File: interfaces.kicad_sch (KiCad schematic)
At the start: 92 parts, among them IC6001 TPD8S009DSMR, J6001 HDMI_A_Female_685119134923, J6002 USB-C_USB4105-GF-A, J6003 MicroSD_693071020811, Q6001 BSS138PW, Q6002 BSS138PW, Q6003 BSS138PW, Q6004 BSS138PW, Q6005 BSS138PW, Q6006 BSS138PW, Q6007 BSS138PW, Q6008 BSS138PW, U6001 FT4232H_VQFN, Y6001 Oscillator_SMD_12MHz_KX-7

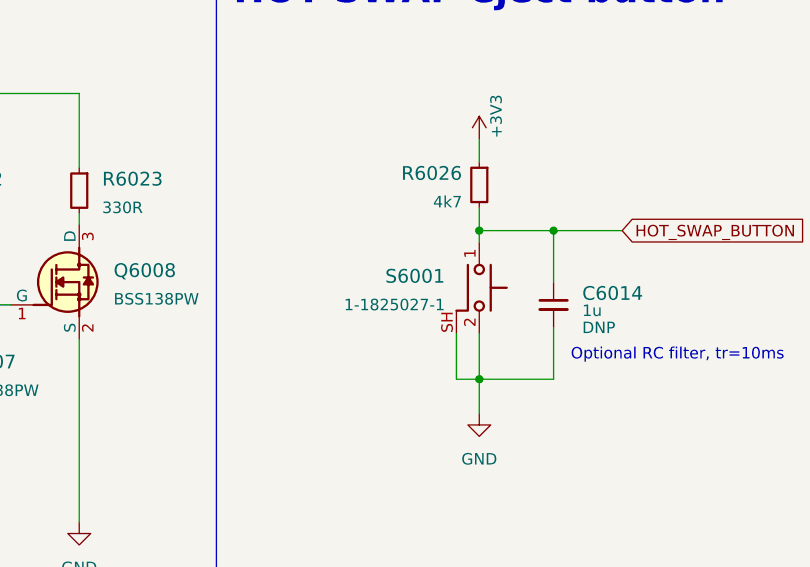
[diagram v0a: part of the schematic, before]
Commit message: Schematic cleanup, connect VINT DC-DC, continue placing misc. circuits
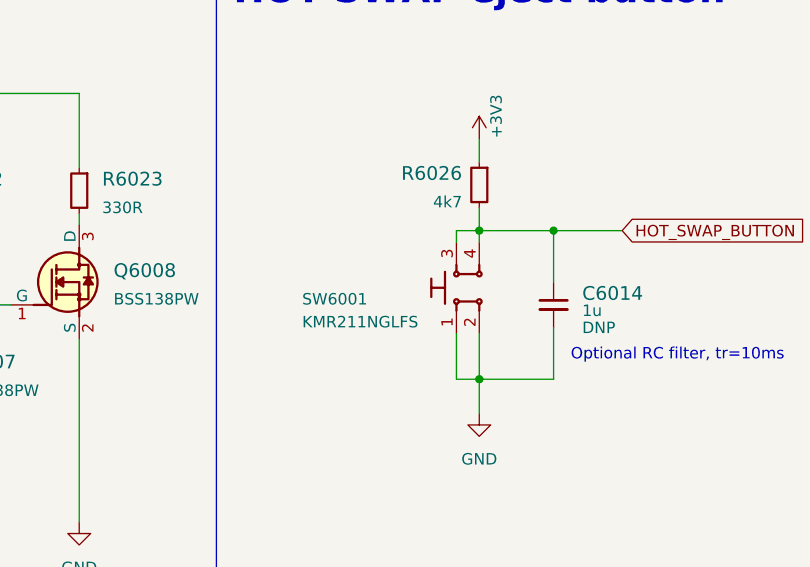
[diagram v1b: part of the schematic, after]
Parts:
- removed S6001: SW_1-1825027-1, data-center-rdimm-ddr4-tester-footprints:SW_Tactile_SPST_Angled_TE_1825027, symbol data-center-rdimm-ddr4-tester:SW_1-1825027-1
- added SW6001: SW_KMR211NGLFS_SMD, antmicro-footprints:SW_KMR211NGLFS_SMD, symbol antmicroPushbuttonSwitches:SW_KMR211NGLFS_SMD
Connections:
- net GND: now also SW6001.1, SW6001.2
- net HOT_SWAP_BUTTON: now also SW6001.3, SW6001.4
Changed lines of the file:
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@@
     (stroke (width 0) (type default) (color 0 0 0 0))
   )
+  (wire (pts (xy 256.54 245.11) (xy 256.54 246.38))
+    (stroke (width 0) (type default) (color 0 0 0 0))
+  )
   (wire (pts (xy 375.92 99.06) (xy 375.92 101.6))
     (stroke (width 0) (type default) (color 0 0 0 0))
@@
     (stroke (width 0) (type default) (color 0 0 0 0))
   )
+  (wire (pts (xy 259.08 245.11) (xy 256.54 245.11))
+    (stroke (width 0) (type default) (color 0 0 0 0))
+  )
   (wire (pts (xy 41.275 74.295) (xy 48.26 74.295))
     (stroke (width 0) (type default) (color 0 0 0 0))
@@
     (pin "SH")
   )
+  (symbol (lib_id "antmicroPushbuttonSwitches:SW_KMR211NGLFS_SMD") (at 256.54 256.54 90) (unit 1)
+    (in_bom yes) (on_board yes)
+    (property "Reference" "SW6001" (id 0) (at 239.395 252.73 90)
+      (effects (font (size 1.27 1.27) (thickness 0.15)) (justify right))
+    )
+    (property "Value" "SW_KMR211NGLFS_SMD" (id 1) (at 264.16 231.14 0)
+      (effects (font (size 1.27 1.27) (thickness 0.15)) (justify left bottom) hide)
+    )
+    (property "Footprint" "antmicro-footprints:SW_KMR211NGLFS_SMD" (id 2) (at 266.7 231.14 0)
+      (effects (font (size 1.27 1.27) (thickness 0.15)) (justify left bottom) hide)
+    )
+    (property "Datasheet" "http://www.farnell.com/datasheets/2631211.pdf" (id 3) (at 269.24 231.14 0)
+      (effects (font (size 1.27 1.27) (thickness 0.15)) (justify left bottom) hide)
+    )
+    (property "MPN" "KMR211NGLFS" (id 4) (at 239.395 255.27 90)
+      (effects (font (size 1.27 1.27) (thickness 0.15)) (justify right))
+    )
+    (property "Manufacturer" "C&K" (id 5) (at 271.78 231.14 0)
+      (effects (font (size 1.27 1.27) (thickness 0.15)) (justify left bottom) hide)
+    )
+    (property "Author" "Antmicro" (id 6) (at 274.32 231.14 0)
+      (effects (font (size 1.27 1.27) (thickness 0.15)) (justify left bottom) hide)
+    )
+    (property "License" "Apache-2.0" (id 7) (at 276.86 231.14 0)
+      (effects (font (size 1.27 1.27) (thickness 0.15)) (justify left bottom) hide)
+    )
+    (pin "1")
+    (pin "2")
+    (pin "3")
+    (pin "4")
+  )
   (symbol (lib_id "power:+3V3") (at 80.645 235.585 90) (unit 1)
     (in_bom yes) (on_board yes)
@@
     (pin "1")
   )
-  (symbol (lib_id "data-center-rdimm-ddr4-tester:SW_1-1825027-1") (at 260.35 246.38 270) (unit 1)
-    (in_bom yes) (on_board yes) (fields_autoplaced)
-    (property "Reference" "S6001" (id 0) (at 255.27 250.19 90)
-      (effects (font (size 1.524 1.524)) (justify right))
-    )
-    (property "Value" "SW_1-1825027-1" (id 1) (at 254.635 253.3649 90)
-      (effects (font (size 1.27 1.27) (thickness 0.15)) (justify right) hide)
-    )
-    (property "Footprint" "data-center-rdimm-ddr4-tester-footprints:SW_Tactile_SPST_Angled_TE_1825027" (id 2) (at 250.19 271.78 0)
-      (effects (font (size 1.27 1.27) (thickness 0.15)) (justify left bottom) hide)
-    )
-    (property "Datasheet" "https://www.te.com/commerce/DocumentDelivery/DDEController?Action=showdoc&DocId=Customer+Drawing%7F1825027%7FH1%7Fpdf%7FEnglish%7FENG_CD_1825027_H1.pdf%7F1-1825027-1" (id 3) (at 247.65 271.78 0)
-      (effects (font (size 1.27 1.27) (thickness 0.15)) (justify left bottom) hide)
-    )
-    (property "MPN" "1-1825027-1" (id 4) (at 255.27 253.3649 90)
-      (effects (font (size 1.27 1.27) (thickness 0.15)) (justify right))
-    )
-    (property "Manufacturer" "TE Connectivity" (id 5) (at 242.57 271.78 0)
-      (effects (font (size 1.27 1.27) (thickness 0.15)) (justify left bottom) hide)
-    )
-    (property "Author" "Antmicro" (id 6) (at 240.03 271.78 0)
-      (effects (font (size 1.27 1.27) (thickness 0.15)) (justify left bottom) hide)
-    )
-    (property "License" "Apache-2.0" (id 7) (at 237.49 271.78 0)
-      (effects (font (size 1.27 1.27) (thickness 0.15)) (justify left bottom) hide)
-    )
-    (pin "1")
-    (pin "2")
-    (pin "SH")
-  )
   (symbol (lib_id "data-center-rdimm-ddr4-tester:BSS138PW") (at 170.18 273.685 0) (unit 1)

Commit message: Add loclib
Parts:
- C6001, C6003, C6005, C6008, C6009, C6010, C6012, C6013, C6016, C6017: footprint data-center-rdimm-ddr4-tester-footprints:C_0402_1005Metric -> sodimm-ddr5-tester-footprints:C_0402_1005Metric; symbol data-center-rdimm-ddr4-tester:C_100n_0402 -> sodimm-ddr5-tester:C_100n_0402
- C6002, C6007: footprint data-center-rdimm-ddr4-tester-footprints:C_0402_1005Metric -> sodimm-ddr5-tester-footprints:C_0402_1005Metric; symbol data-center-rdimm-ddr4-tester:C_18p_0402 -> sodimm-ddr5-tester:C_18p_0402
- C6004, C6006, C6011: footprint data-center-rdimm-ddr4-tester-footprints:C_0402_1005Metric -> sodimm-ddr5-tester-footprints:C_0402_1005Metric; symbol data-center-rdimm-ddr4-tester:C_4u7_0402 -> sodimm-ddr5-tester:C_4u7_0402
- C6014, C6015: footprint data-center-rdimm-ddr4-tester-footprints:C_0402_1005Metric -> sodimm-ddr5-tester-footprints:C_0402_1005Metric; symbol data-center-rdimm-ddr4-tester:C_1u_0402 -> sodimm-ddr5-tester:C_1u_0402
- D6001, D6002, D6003, D6004, D6005: footprint data-center-rdimm-ddr4-tester-footprints:LED_0603_1608Metric_G -> sodimm-ddr5-tester-footprints:LED_0603_1608Metric_G; symbol data-center-rdimm-ddr4-tester:LED_G_0603_KP-1608CGCK -> sodimm-ddr5-tester:LED_G_0603_KP-1608CGCK
- D6006: footprint data-center-rdimm-ddr4-tester-footprints:LED_RGY_1.6x1.6mm_APTF1616 -> sodimm-ddr5-tester-footprints:LED_RGY_1.6x1.6mm_APTF1616; symbol data-center-rdimm-ddr4-tester:LED_RGY_0606_APTF1616SURKCGKSYKC -> sodimm-ddr5-tester:LED_RGY_0606_APTF1616SURKCGKSYKC
- D6007: footprint data-center-rdimm-ddr4-tester-footprints:SOT-723 -> sodimm-ddr5-tester-footprints:SOT-723; symbol data-center-rdimm-ddr4-tester:TPD2E009_SOT-9X3 -> sodimm-ddr5-tester:TPD2E009_SOT-9X3
- FB6001, FB6002: footprint data-center-rdimm-ddr4-tester-footprints:FB_0603_1608Metric -> sodimm-ddr5-tester-footprints:FB_0603_1608Metric; symbol data-center-rdimm-ddr4-tester:FB_600Z_0.5A_0603 -> sodimm-ddr5-tester:FB_600Z_0.5A_0603
- IC6001: footprint data-center-rdimm-ddr4-tester-footprints:R-PDSO-N15 -> sodimm-ddr5-tester-footprints:R-PDSO-N15; symbol data-center-rdimm-ddr4-tester:TPD8S009DSMR -> sodimm-ddr5-tester:TPD8S009DSMR
- J6001: footprint data-center-rdimm-ddr4-tester-footprints:HDMI-A_Wurth_685119134923 -> sodimm-ddr5-tester-footprints:HDMI-A_Wurth_685119134923; symbol data-center-rdimm-ddr4-tester:HDMI_A_Female_685119134923 -> sodimm-ddr5-tester:HDMI_A_Female_685119134923
- J6002: footprint data-center-rdimm-ddr4-tester-footprints:USB-C_GCT_USB4105-GF-A -> sodimm-ddr5-tester-footprints:USB-C_GCT_USB4105-GF-A; symbol data-center-rdimm-ddr4-tester:USB-C_USB4105-GF-A -> sodimm-ddr5-tester:USB-C_USB4105-GF-A
- J6003: footprint data-center-rdimm-ddr4-tester-footprints:MicroSD_Wurth_693071020811 -> sodimm-ddr5-tester-footprints:MicroSD_Wurth_693071020811; symbol data-center-rdimm-ddr4-tester:MicroSD_693071020811 -> sodimm-ddr5-tester:MicroSD_693071020811
- Q6001, Q6002, Q6003, Q6004, Q6005, Q6006, Q6007, Q6008: footprint data-center-rdimm-ddr4-tester-footprints:SC70-3 -> sodimm-ddr5-tester-footprints:SC70-3; symbol data-center-rdimm-ddr4-tester:BSS138PW -> sodimm-ddr5-tester:BSS138PW
- R6001, R6002, R6003, R6006, R6007, R6021, R6022, R6023, R6043, R6044: footprint data-center-rdimm-ddr4-tester-footprints:R_0402_1005Metric -> sodimm-ddr5-tester-footprints:R_0402_1005Metric; symbol data-center-rdimm-ddr4-tester:R_330R_0402 -> sodimm-ddr5-tester:R_330R_0402
- R6004: footprint data-center-rdimm-ddr4-tester-footprints:R_0402_1005Metric -> sodimm-ddr5-tester-footprints:R_0402_1005Metric; symbol data-center-rdimm-ddr4-tester:R_10k_0402 -> sodimm-ddr5-tester:R_10k_0402
- R6005: footprint data-center-rdimm-ddr4-tester-footprints:R_0402_1005Metric -> sodimm-ddr5-tester-footprints:R_0402_1005Metric; symbol data-center-rdimm-ddr4-tester:R_12k_0402 -> sodimm-ddr5-tester:R_12k_0402
- R6008, R6009, R6010, R6011, R6012, R6013, R6014, R6015, R6016, R6017, R6018, R6019, R6020: footprint data-center-rdimm-ddr4-tester-footprints:R_0402_1005Metric -> sodimm-ddr5-tester-footprints:R_0402_1005Metric; symbol data-center-rdimm-ddr4-tester:R_22R_0402 -> sodimm-ddr5-tester:R_22R_0402
- R6024, R6025: footprint data-center-rdimm-ddr4-tester-footprints:R_0402_1005Metric -> sodimm-ddr5-tester-footprints:R_0402_1005Metric; symbol data-center-rdimm-ddr4-tester:R_5k11_0402 -> sodimm-ddr5-tester:R_5k11_0402
- R6026: footprint data-center-rdimm-ddr4-tester-footprints:R_0402_1005Metric -> sodimm-ddr5-tester-footprints:R_0402_1005Metric; symbol data-center-rdimm-ddr4-tester:R_4k7_0402 -> sodimm-ddr5-tester:R_4k7_0402
- R6027, R6028, R6029, R6030, R6032, R6035, R6038, R6041: footprint data-center-rdimm-ddr4-tester-footprints:R_0402_1005Metric -> sodimm-ddr5-tester-footprints:R_0402_1005Metric; symbol data-center-rdimm-ddr4-tester:R_0R_0402 -> sodimm-ddr5-tester:R_0R_0402
- R6031, R6033, R6034, R6036, R6039, R6040, R6042: footprint data-center-rdimm-ddr4-tester-footprints:R_0402_1005Metric -> sodimm-ddr5-tester-footprints:R_0402_1005Metric; symbol data-center-rdimm-ddr4-tester:R_20k_0402 -> sodimm-ddr5-tester:R_20k_0402
- R6037: footprint data-center-rdimm-ddr4-tester-footprints:R_0402_1005Metric -> sodimm-ddr5-tester-footprints:R_0402_1005Metric; symbol data-center-rdimm-ddr4-tester:R_220R_0402 -> sodimm-ddr5-tester:R_220R_0402
- SW6001: footprint antmicro-footprints:SW_KMR211NGLFS_SMD -> sodimm-ddr5-tester-footprints:SW_KMR211NGLFS_SMD; symbol antmicroPushbuttonSwitches:SW_KMR211NGLFS_SMD -> sodimm-ddr5-tester:SW_KMR211NGLFS_SMD
- TP6001, TP6002, TP6003, TP6004, TP6005, TP6006, VBUS6001: footprint data-center-rdimm-ddr4-tester-footprints:Testpoint_smd_1mm -> sodimm-ddr5-tester-footprints:Testpoint_smd_1mm; symbol data-center-rdimm-ddr4-tester:TP_1mm_SMD -> sodimm-ddr5-tester:TP_1mm_SMD
- U6001: footprint data-center-rdimm-ddr4-tester-footprints:QFN-56-1EP_8x8mm_P0.5mm -> sodimm-ddr5-tester-footprints:QFN-56-1EP_8x8mm_P0.5mm; symbol data-center-rdimm-ddr4-tester:FT4232H_VQFN -> sodimm-ddr5-tester:FT4232H_VQFN
- Y6001: footprint data-center-rdimm-ddr4-tester-footprints:Oscillator_SMD_Geyer_KX-7-4Pin_3.2x2.5mm -> sodimm-ddr5-tester-footprints:Oscillator_SMD_Geyer_KX-7-4Pin_3.2x2.5mm; symbol data-center-rdimm-ddr4-tester:Oscillator_SMD_12MHz_KX-7 -> sodimm-ddr5-tester:Oscillator_SMD_12MHz_KX-7

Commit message: Bump revision to 1.0.0
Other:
- title: LPDDR5 Test Board -> SO-DIMM DDR5 Tester

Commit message: Connect RFU, start improving interfaces and supply sheet, unify ESD protection
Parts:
- removed D6007: TPD2E009_SOT-9X3, sodimm-ddr5-tester-footprints:SOT-723, symbol sodimm-ddr5-tester:TPD2E009_SOT-9X3
- removed IC6001: TPD8S009DSMR, sodimm-ddr5-tester-footprints:R-PDSO-N15, symbol sodimm-ddr5-tester:TPD8S009DSMR
- removed J6001: HDMI_A_Female_685119134923, sodimm-ddr5-tester-footprints:HDMI-A_Wurth_685119134923, symbol sodimm-ddr5-tester:HDMI_A_Female_685119134923
- added C?: C_10u_25V_0603, antmicro-footprints:C_0603_1608Metric, symbol antmicroCapacitors0603:C_10u_25V_0603
- added C? (x2): C_100n_0402_EIA, K410T-devboard-footprints:C_0402_1005Metric_EIA, symbol K410T-devboard:C_100n_0402_EIA
- added C?: C_10u_0402, antmicro-footprints:C_0402_1005Metric, symbol antmicroCapacitors0402:C_10u_0402
- added D? (x2): BAT54-02V-G3-08, antmicro-footprints:SOD-523, symbol antmicroDiodesRectifiersSingle:BAT54-02V-G3-08
- added D? (x4): LED_G_0603_KP-1608CGCK, sodimm-ddr5-tester-footprints:LED_0603_1608Metric_G, symbol sodimm-ddr5-tester:LED_G_0603_KP-1608CGCK
- added FB?: FB_120Z_2A_0603, K410T-devboard-footprints:FB_0603_1608Metric, symbol K410T-devboard:FB_120Z_2A_0603
- added J6001: HDMI-A_WE_685119134923, antmicro-footprints:HDMI-A_Receptacle_WE_685119134923, symbol antmicroVideoConnectors:HDMI-A_WE_685119134923
- added R? (x4): R_0R_0402, antmicro-footprints:R_0402_1005Metric, symbol antmicroResistors0402:R_0R_0402
- added R? (x4): R_330R_0402, antmicro-footprints:R_0402_1005Metric, symbol antmicroResistors0402:R_330R_0402
- added R?: R_47k_0402, antmicro-footprints:R_0402_1005Metric, symbol antmicroResistors0402:R_47k_0402
- added R?: R_10k_0402, antmicro-footprints:R_0402_1005Metric, symbol antmicroResistors0402:R_10k_0402
- added U? (x2): TXU0304BQAR, antmicro-footprints:DHVQFN-14_1EP_2.5x3mm, symbol antmicroLogicTranslatorsLevelShifters:TXU0304BQAR
- added U?: NCP718BSN330T1G, antmicro-footprints:SOT-23-5, symbol antmicroPMICVoltageRegulatorsLinear:NCP718BSN330T1G
- added U? (x3): TPD4E05U06QDQARQ1, antmicro-footprints:USON-10_2.5x1mm_P0.5mm, symbol antmicroTVSDiodes:TPD4E05U06QDQARQ1
- added U?: SN74HC595B, antmicro-footprints:X1QFN-16-1EP_2.5x2.5mm, symbol antmicroLogicShiftRegisters:SN74HC595B
- R6012, R6013, R6014, R6015, R6016: DNP (none) -> DNP
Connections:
- net +3V3: now also R?.2, U?.14 (VCCB), U?.14 (VCCB); no longer FB6001.1, FB6002.1, R6004.1, U6001.16 (V_{CCIO}), U6001.36 (V_{CCIO}), U6001.44 (V_{REGIN}), U6001.50 (V_{CCIO})
- net DBG_USB_N: now also U?.2, U?.9
- net DBG_USB_P: now also U?.1, U?.10
- net GND: now also C?.1, C?.1, C?.1, C?.1, D?.2, D?.2, D?.2, D?.2, J6001.11 (CKS), J6001.17 (GND), J6001.2 (D2S), J6001.5 (D1S), J6001.8 (D0S), U?.15 (GND), U?.15 (GND), U?.2 (GND), U?.3, U?.3, U?.3, U?.3 (A2), U?.7 (GND), U?.7 (GND), U?.8, U?.8, U?.8, U?.8 (GND)
- net GND1: now also J6001.SH
- net VBUS: now also C?.2, U?.1 (VIN), U?.3 (EN)
- net BDBUS0: now reaches R6012.1, U6001.22 (BDBUS0)
- net BDBUS0: now also U?.2 (A1)
- net BDBUS1: now reaches R6013.1, U6001.23 (BDBUS1)
- net BDBUS1: now also U?.4 (A3)
- net BDBUS2: now reaches R6014.1, U6001.24 (BDBUS2)
- net BDBUS2: now also U?.5 (A4Y)
- net BDBUS3: now reaches R6015.1, U6001.25 (BDBUS3)
- net BDBUS3: now also R?.2
- net I2C_EN: now reaches R6016.1, U6001.27 (BDBUS5)
- net I2C_EN: now also R?.1
- net at TP6002.1: now also J6001.13 (CEC)
- net at TP6003.1: now also J6001.15 (SCL)
- net at TP6005.1: now also J6001.16 (SDA)
- net HDMI_CONN_5V: now reaches TP6006.1
- net HDMI_CONN_5V: now also D?.1, J6001.18 (+5V)
- net at TP6004.1: now also J6001.19 (HPD/HEAC-)
- net at R6008.1: now also U?.13 (B1Y); no longer U6001.12 (ADBUS0)
- net at R6009.1: now also U?.11 (B3Y); no longer U6001.13 (ADBUS1)
- net at R6010.1: now also U?.10 (B4); no longer U6001.14 (ADBUS2)
- net at R6011.1: now also U?.12 (B2Y); no longer U6001.15 (ADBUS3)
- net FTDI_JTAG_RST: now reaches TP6001.1, U6001.18 (ADBUS5)
- net FTDI_EECS: now reaches U6001.1 (EECS)
- net FTDI_EECS: now also U?.12 (RCLK)
- net SPI_EN: now reaches U6001.26 (BDBUS4)
- net FTDI_PWREN: now reaches U6001.54 (~{PWR_{EN}})
- net FTDI_PWREN: now also R?.2, U?.13 (~{OE})
- net FTDI_EEDAT: now reaches U6001.55 (EEDATA)
- net FTDI_EEDAT: now also U?.14 (SER)
- net FTDI_EECLK: now reaches U6001.56 (EECLK)
- net FTDI_EECLK: now also U?.11 (SRCLK)
- net C_TMDS_CLK_N renamed HDMI_CONN_CLK_N
- net HDMI_CONN_CLK_N: now also J6001.12 (CK-), U?.5, U?.6
- net C_TMDS_CLK_P renamed HDMI_CONN_CLK_P
- net HDMI_CONN_CLK_P: now also J6001.10 (CK+), U?.4, U?.7
- net C_TMDS_D0_N renamed HDMI_CONN_D0_N
- net HDMI_CONN_D0_N: now also J6001.9 (D0-), U?.2, U?.9
- net C_TMDS_D0_P renamed HDMI_CONN_D0_P
- net HDMI_CONN_D0_P: now also J6001.7 (D0+), U?.1, U?.10
- net C_TMDS_D1_N renamed HDMI_CONN_D1_N
- net HDMI_CONN_D1_N: now also J6001.6 (D1-), U?.5, U?.6
- net C_TMDS_D1_P renamed HDMI_CONN_D1_P
- net HDMI_CONN_D1_P: now also J6001.4 (D1+), U?.4, U?.7
- net C_TMDS_D2_N renamed HDMI_CONN_D2_N
- net HDMI_CONN_D2_N: now also J6001.3 (D2-), U?.2, U?.9
- net C_TMDS_D2_P renamed HDMI_CONN_D2_P
- net HDMI_CONN_D2_P: now also J6001.1 (D2+), U?.1, U?.10
- new net: R?.1, R?.2, U?.8 (OE)
- new net: D?.1, R?.1 (x4)
- new net: U?.4, U?.7
- new net: U?.5, U?.6
- new net +5V: FB?.1
- new net FTDI_3V3: C?.2, C?.2, FB6001.1, FB6002.1, R6004.1, R?.1, U6001.16 (V_{CCIO}), U6001.36 (V_{CCIO}), U6001.44 (V_{REGIN}), U6001.50 (V_{CCIO}), U?.1 (VCCA), U?.1 (VCCA), U?.10 (~{SRCLR}), U?.16 (VCC), U?.5 (VOUT)
- new net FTDI_DIS: R?.1, U?.8 (OE)
- new net FTDI_JTAG_TCK: U6001.12 (ADBUS0), U?.2 (A1)
- new net FTDI_JTAG_TDI: U6001.13 (ADBUS1), U?.4 (A3)
- new net FTDI_JTAG_TDO: U6001.14 (ADBUS2), U?.5 (A4Y)
- new net FTDI_JTAG_TMS: U6001.15 (ADBUS3), U?.3 (A2)
- new net FTDI_SCL: R?.1, U?.13 (B1Y)
- new net FTDI_SCL_3V3: R?.2
- new net FTDI_SDA_3V3: R?.1
- new net FTDI_SDA_IN: D?.2, R?.2, U?.10 (B4)
- new net FTDI_SDA_OUT: D?.1, U?.11 (B3Y)
- new net HDMI_5V: C?.2, D?.2, FB?.2
- new net LED_RX0: R?.2, U?.5 (QF)
- new net LED_RX1: R?.2, U?.7 (QH)
- new net LED_TX0: R?.2, U?.4 (QE)
- new net LED_TX1: R?.2, U?.6 (QG)
- no-connect marks 26 -> 29
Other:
- note added: "I2C_SCL"
- note added: "I2C_SDA_IN"
- note added: "I2C_SDA_OUT"
- moved on the sheet: R6008, R6009, R6010, R6011, R6012, R6013, R6014, R6015, R6016, R6027, R6028, R6029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
